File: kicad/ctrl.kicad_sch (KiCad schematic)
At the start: 10 parts, among them U11 74LS245, U13 74LS244, U14 74LS244, U15 74LS244, U16 74LS244, U17 74LS670, U18 74LS373, U3 74LS27, U45 74LS04, U6 74LS00

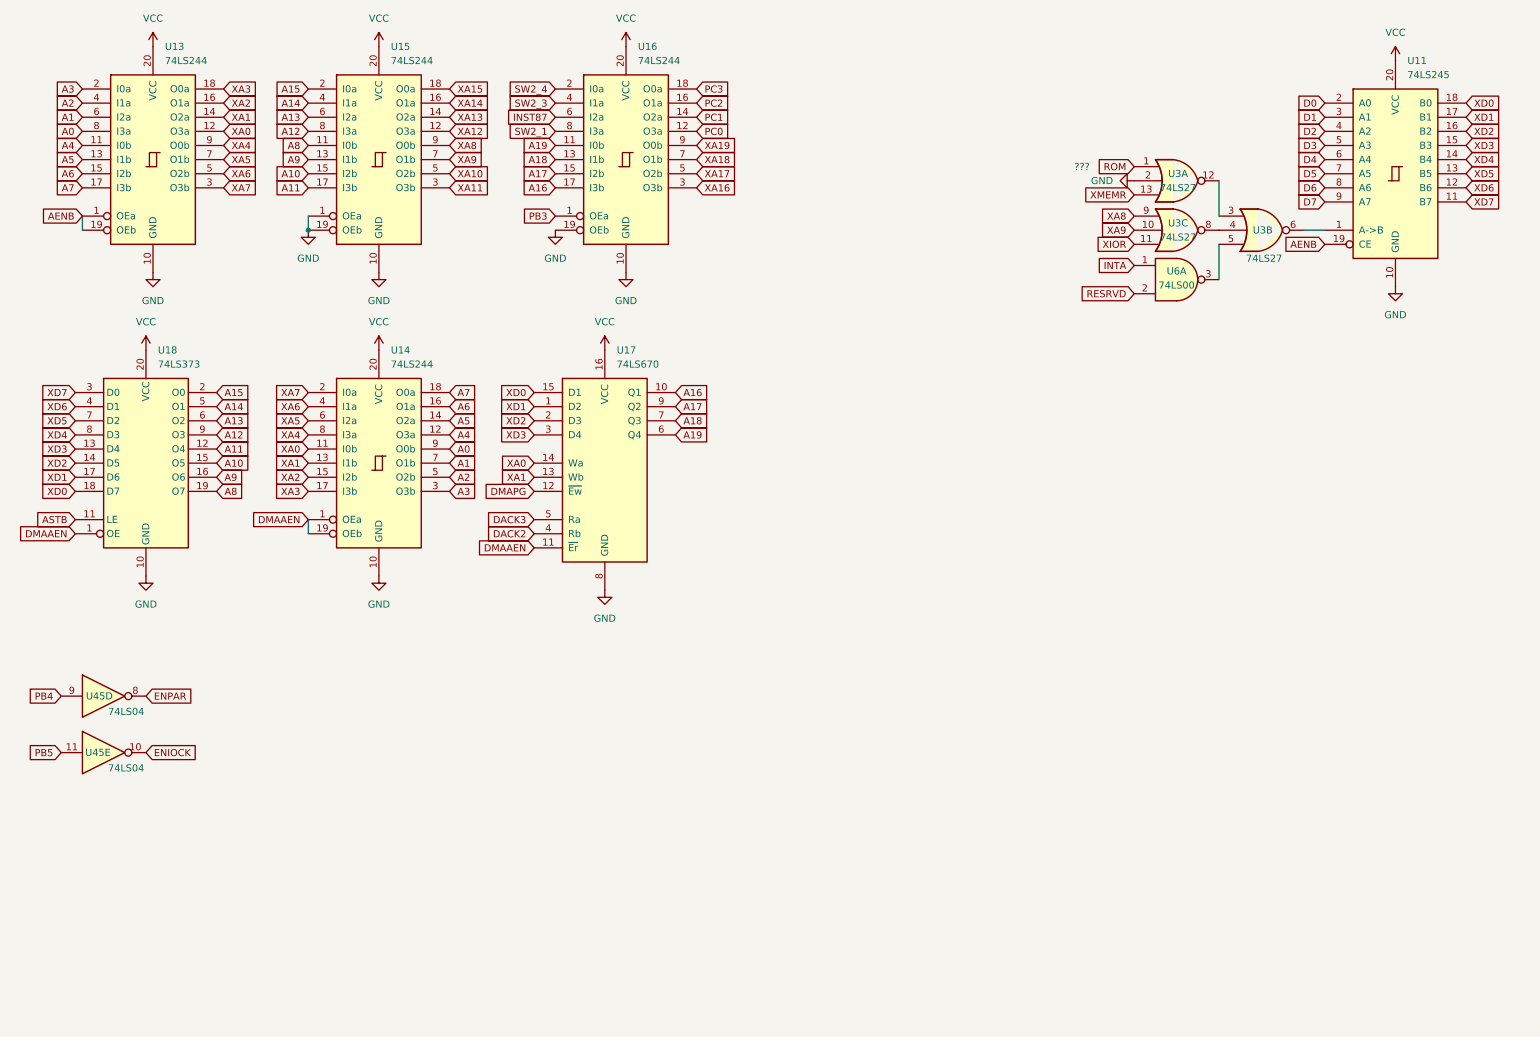
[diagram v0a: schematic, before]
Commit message: finalized schematic
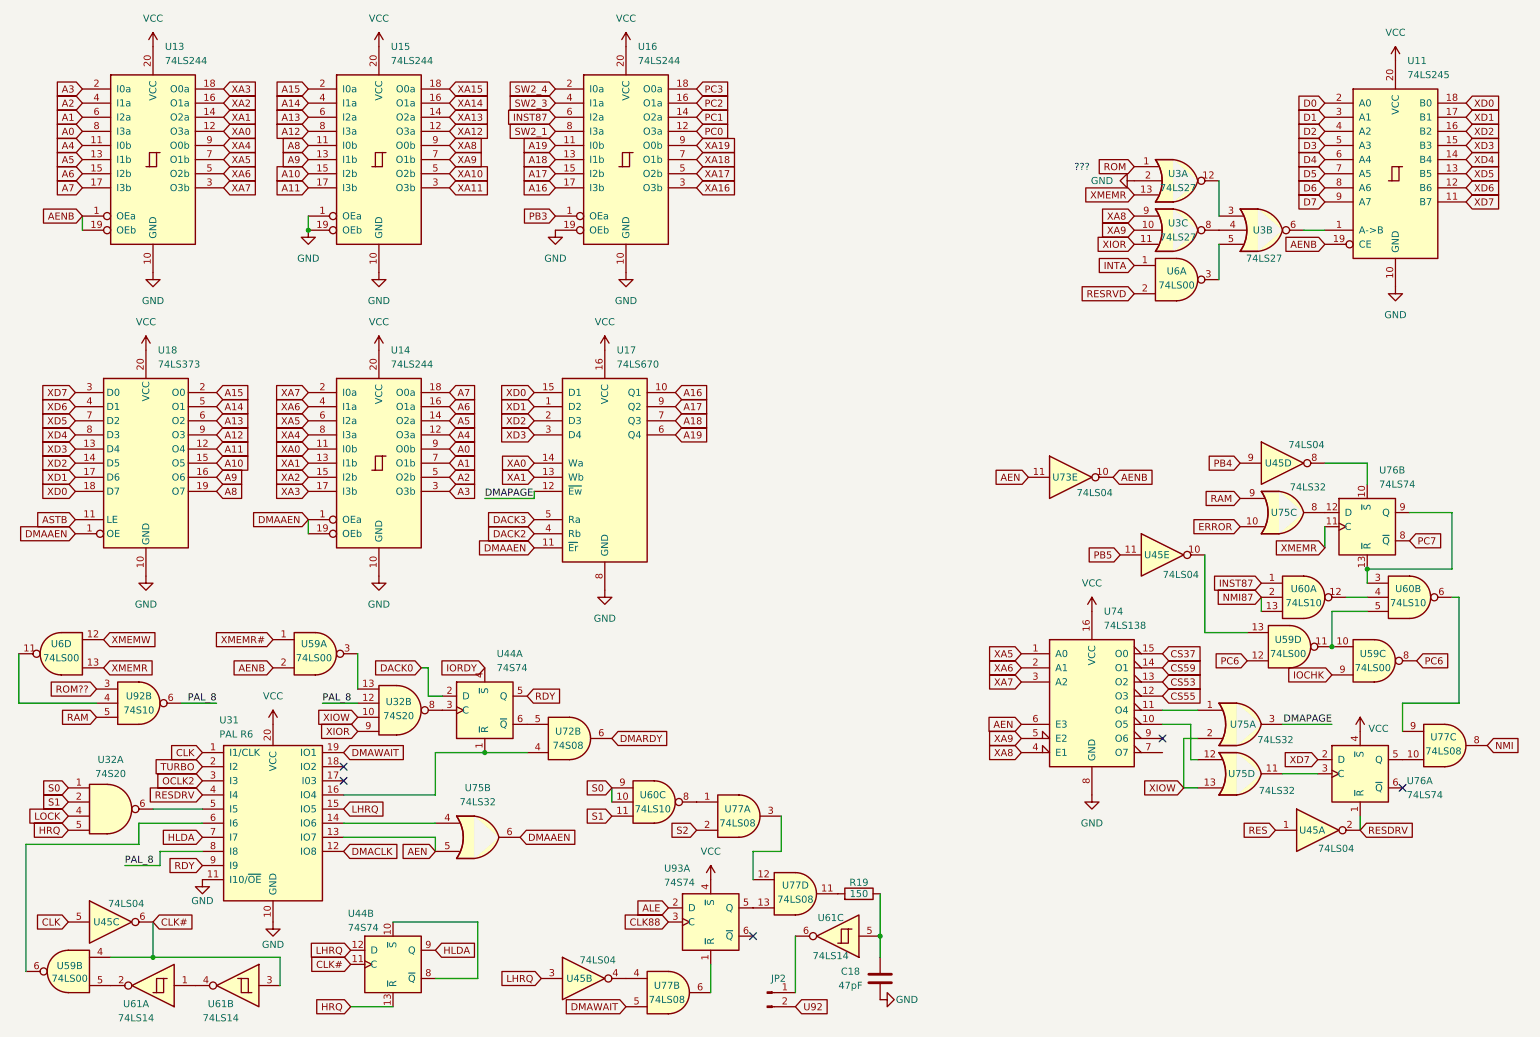
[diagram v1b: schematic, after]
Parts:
- added C18: 47pF, Capacitor_THT:C_Disc_D3.0mm_W1.6mm_P2.50mm, symbol Device:C
- added JP2: Conn_01x02_Pin, symbol Connector:Conn_01x02_Pin
- added R19: 150, Resistor_THT:R_Axial_DIN0204_L3.6mm_D1.6mm_P7.62mm_Horizontal, symbol Device:R
- added U31: PAL R6, symbol Logic_Programmable:GAL16V8
- added U32: 74S20, symbol 74xx:74LS20
- added U44: 74S74, symbol 74xx:74LS74
- added unit 1 of U45
- added unit 3 of U45
- added unit 2 of U45
- added U59: 74LS00, Package_DIP:DIP-14_W7.62mm, symbol 74xx:74LS00
- added unit 4 of U6
- added U60: 74LS10, Package_DIP:DIP-14_W7.62mm, symbol 74xx:74LS10
- added U61: 74LS14, Package_DIP:DIP-14_W7.62mm, symbol 74xx:74LS14
- added U72: 74S08, Package_DIP:DIP-14_W7.62mm, symbol 74xx:74LS08
- added U73: 74LS04, Package_DIP:DIP-14_W7.62mm, symbol 74xx:74LS04
- added U74: 74LS138, Package_DIP:DIP-16_W7.62mm, symbol 74xx:74LS138
- added U75: 74LS32, Package_DIP:DIP-14_W7.62mm, symbol 74xx:74LS32
- added U76: 74LS74, Package_DIP:DIP-14_W7.62mm, symbol 74xx:74LS74
- added U77: 74LS08, Package_DIP:DIP-14_W7.62mm, symbol 74xx:74LS08
- added U92: 74S10, Package_DIP:DIP-14_W7.62mm, symbol 74xx:74LS10
- added U93: 74S74, Package_DIP:DIP-14_W7.62mm, symbol 74xx:74LS74
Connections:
- net AENB: now also U59.2, U73.10
- net DMAAEN: now also U75.6
- net GND: now also C18.1, U31.10 (GND), U31.11 (I10/~{OE}), U74.8 (GND)
- net INST87: now also U60.1
- net VCC: now also U31.20 (VCC), U74.16 (VCC), U76.4 (~{S}), U93.4 (~{S})
- net XA5: now also U74.1 (A0)
- net XA6: now also U74.2 (A1)
- net XA7: now also U74.3 (A2)
- net XA8: now also U74.4 (E1)
- net XA9: now also U74.5 (E2)
- net XD7: now also U76.2 (D)
- net XIOR: now also U32.9
- net XMEMR: now also U6.13, U76.11 (C)
- net DMAPG renamed DMAPAGE
- net DMAPAGE: now also U75.3
- net ENIOCK: no longer names the net of U45.10
- net ENIOCK: now also U59.13
- net ENPAR: no longer names the net of U45.8
- net ENPAR: now also U76.10 (~{S})
- new net: U31.14 (IO6), U75.4
- new net: U75.11, U76.3 (C)
- new net: U74.10 (O5), U75.12
- new net: U6.11, U92.4
- new net: U32.13, U59.3
- new net: U32.8, U44.3 (C)
- new net: U61.1, U61.4
- new net: U31.16 (IO4), U44.1 (~{R}), U72.4
- new net: U44.6 (~{Q}), U72.5
- new net: U59.10, U59.11, U60.5
- new net: U74.11 (O4), U75.1
- new net: U45.4, U77.4
- new net: U77.6, U93.1 (~{R})
- new net: U75.8, U76.12 (D)
- new net: U60.3, U76.13 (~{R}), U76.9 (Q)
- new net: U60.12, U60.4
- new net: U60.6, U77.9
- new net: U59.5, U61.2
- new net: U76.5 (Q), U77.10
- new net: U60.8, U77.1
- new net: U31.6 (I6), U59.6
- new net: C18.2, R19.1, U61.5
- new net: R19.2, U77.11
- new net: U31.5 (I5), U32.6
- new net: U77.12, U77.3
- new net: JP2.1 (Pin_1), U61.6
- new net: U44.10 (~{S}), U44.8 (~{Q})
- new net: U77.13, U93.5 (Q)
- new net AEN: U31.13 (IO7), U73.11, U74.6 (E3), U75.5
- new net ALE: U93.2 (D)
- new net CLK: U31.1 (I1/CLK), U45.5
- new net CLK#: U44.11 (C), U45.6, U59.4, U61.3
- new net CLK88: U93.3 (C)
- new net CS37: U74.15 (O0)
- new net CS53: U74.13 (O2)
- new net CS55: U74.12 (O3)
- new net CS59: U74.14 (O1)
- new net DACK0: U44.2 (D)
- new net DMACLK: U31.12 (IO8)
- new net DMARDY: U72.6
- new net DMAWAIT: U31.19 (IO1), U77.5
- new net ERROR: U75.10
- new net HLDA: U31.7 (I7), U44.9 (Q)
- new net HRQ: U32.5, U44.13 (~{R})
- new net IOCHK: U59.9
- new net IORDY: U44.4 (~{S})
- new net LHRQ: U31.15 (IO5), U44.12 (D), U45.3
- new net LOCK: U32.4
- new net NMI: U77.8
- new net NMI87: U60.13, U60.2
- new net OCLK2: U31.3 (I3)
- new net PAL_8: U31.8 (I8), U32.12, U92.6
- new net PC6: U59.12, U59.8
- new net PC7: U76.8 (~{Q})
- new net RAM: U75.9, U92.5
- new net RDY: U31.9 (I9), U44.5 (Q)
- new net RES: U45.1
- new net RESDRV: U31.4 (I4), U45.2, U76.1 (~{R})
- new net ROM??: U92.3
- new net S0: U32.1, U60.10, U60.9
- new net S1: U32.2, U60.11
- new net S2: U77.2
- new net TURBO: U31.2 (I2)
- new net U92: JP2.2 (Pin_2)
- new net XIOW: U32.10, U75.13, U75.2
- new net XMEMR#: U59.1
- new net XMEMW: U6.12
- no-connect marks 0 -> 5
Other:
- moved on the sheet: U45D, U45E
